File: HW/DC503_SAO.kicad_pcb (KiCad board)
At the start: 2 copper layers, 63.1 x 45.1 mm, 34 parts, among them J1 GS2, J2 GS2, U1 ATTINY85-20SU, X1 Badgelife_shitty_connector

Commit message: ROW3 and ROW_3 done.
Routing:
- net /ROW2: track 35.8 -> 90.4 mm, vias 0 -> 5
- net /ROW3: track 35.9 -> 85.7 mm
- net /ROW_2: track 73.2 -> 73.4 mm, vias 2 -> 4
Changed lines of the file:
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@@
   (general
     (links 38)
-    (no_connects 8)
+    (no_connects 4)
     (area 142.865544 64.023399 206.110001 109.234705)
     (thickness 1.6002)
     (drawings 335)
-    (tracks 141)
+    (tracks 170)
     (zones 0)
     (modules 34)
@@
     (37 F.SilkS user)
     (38 B.Mask user)
-    (39 F.Mask user)
+    (39 F.Mask user hide)
     (40 Dwgs.User user)
     (41 Cmts.User user)
@@
   (gr_line (start 205.4289 69.7478) (end 205.4621 69.7962) (layer Edge.Cuts) (width 0.1))
   (gr_line (start 204.5 75.5) (end 204.3829 75.8431) (layer Edge.Cuts) (width 0.1))
+  (segment (start 180 104.25) (end 176.25 104.25) (width 0.3048) (layer B.Cu) (net 1) (status 400000))
+  (via (at 156.6 100.2) (size 0.6858) (drill 0.3302) (layers F.Cu B.Cu) (net 1))
+  (segment (start 156.6 103.6) (end 156.6 100.2) (width 0.3048) (layer B.Cu) (net 1))
+  (segment (start 161.6 108.4) (end 156.6 103.6) (width 0.3048) (layer B.Cu) (net 1))
+  (segment (start 174.2 108.4) (end 161.6 108.4) (width 0.3048) (layer B.Cu) (net 1))
+  (via (at 174.2 108.4) (size 0.6858) (drill 0.3302) (layers F.Cu B.Cu) (net 1))
+  (segment (start 174.2 106.2) (end 174.2 108.4) (width 0.3048) (layer F.Cu) (net 1))
+  (segment (start 176.2 104.2) (end 174.2 106.2) (width 0.3048) (layer F.Cu) (net 1))
+  (via (at 176.2 104.2) (size 0.6858) (drill 0.3302) (layers F.Cu B.Cu) (net 1))
+  (segment (start 176.25 104.25) (end 176.2 104.2) (width 0.3048) (layer B.Cu) (net 1))
+  (segment (start 156.6 95.2) (end 156.6 100.2) (width 0.3048) (layer F.Cu) (net 1))
+  (segment (start 156.6 100.2) (end 156.6 97.8) (width 0.3048) (layer F.Cu) (net 1))
+  (via (at 156.6 95.2) (size 0.6858) (drill 0.3302) (layers F.Cu B.Cu) (net 1))
+  (segment (start 147.25 98.55) (end 147.25 93.25) (width 0.3048) (layer B.Cu) (net 1) (status 800000))
+  (segment (start 147.2 98.8) (end 147.25 98.55) (width 0.3048) (layer B.Cu) (net 1))
+  (via (at 147.2 98.8) (size 0.6858) (drill 0.3302) (layers F.Cu B.Cu) (net 1))
+  (segment (start 155.6 98.8) (end 147.2 98.8) (width 0.3048) (layer F.Cu) (net 1))
+  (segment (start 156.6 97.8) (end 155.6 98.8) (width 0.3048) (layer F.Cu) (net 1))
   (segment (start 150 70.5) (end 150 76.8) (width 0.3048) (layer B.Cu) (net 1))
-  (segment (start 147.25 79.55) (end 147.25 93.25) (width 0.3048) (layer B.Cu) (net 1))
   (segment (start 150 76.8) (end 147.25 79.55) (width 0.3048) (layer B.Cu) (net 1))
+  (segment (start 147.25 79.55) (end 147.25 93.25) (width 0.3048) (layer B.Cu) (net 1))
   (segment (start 159.25 88.2) (end 159.25 89.25) (width 0.3048) (layer B.Cu) (net 1))
   (segment (start 159.25 89.25) (end 159 89.5) (width 0.3048) (layer B.Cu) (net 1))
@@
   (segment (start 156.25 94.5) (end 156.6 95.2) (width 0.3048) (layer B.Cu) (net 1))
   (segment (start 156.6 95.2) (end 159.1 95.235) (width 0.3048) (layer B.Cu) (net 1))
-  (segment (start 163.5 75) (end 163.5 83.3) (width 0.3048) (layer B.Cu) (net 2))
+  (segment (start 192.5 81.75) (end 192.5 79.1) (width 0.3048) (layer B.Cu) (net 2) (status 400000))
+  (segment (start 191.2 77.8) (end 163.5 77.8) (width 0.3048) (layer B.Cu) (net 2))
+  (segment (start 192.5 79.1) (end 191.2 77.8) (width 0.3048) (layer B.Cu) (net 2))
+  (segment (start 148.75 81.75) (end 148.75 79.65) (width 0.3048) (layer B.Cu) (net 2) (status 400000))
+  (segment (start 150.6 77.8) (end 163.5 77.8) (width 0.3048) (layer B.Cu) (net 2))
+  (segment (start 148.75 79.65) (end 150.6 77.8) (width 0.3048) (layer B.Cu) (net 2))
+  (segment (start 163.5 75) (end 163.5 77.8) (width 0.3048) (layer B.Cu) (net 2))
+  (segment (start 163.5 77.8) (end 163.5 83.3) (width 0.3048) (layer B.Cu) (net 2))
   (segment (start 161.4 85.4) (end 161.4 91) (width 0.3048) (layer B.Cu) (net 2))
   (segment (start 163.5 83.3) (end 161.4 85.4) (width 0.3048) (layer B.Cu) (net 2))
@@
   (segment (start 153.25 99.35) (end 153.25 93.25) (width 0.3048) (layer B.Cu) (net 11))
   (segment (start 152.25 100.35) (end 153.25 99.35) (width 0.3048) (layer B.Cu) (net 11))
-  (segment (start 157.2 72.2) (end 157.2 80.8) (width 0.3048) (layer B.Cu) (net 12))
-  (via (at 157.2 80.8) (size 0.6858) (drill 0.3302) (layers F.Cu B.Cu) (net 12))
+  (segment (start 157.2 72.2) (end 157.2 76.4) (width 0.3048) (layer B.Cu) (net 12))
+  (via (at 157.2 76.4) (size 0.6858) (drill 0.3302) (layers F.Cu B.Cu) (net 12))
   (segment (start 156.3 86.3) (end 155.25 86.3) (width 0.3048) (layer B.Cu) (net 12))
   (via (at 157.2 85.6) (size 0.6858) (drill 0.3302) (layers F.Cu B.Cu) (net 12))
   (segment (start 156.3 86.3) (end 157.2 85.6) (width 0.3048) (layer B.Cu) (net 12))
-  (segment (start 157.2 80.8) (end 157.2 85.6) (width 0.3048) (layer F.Cu) (net 12))
+  (segment (start 157.2 76.4) (end 157.2 85.6) (width 0.3048) (layer F.Cu) (net 12))
   (segment (start 157.2 72.2) (end 157.2 72.3375) (width 0.3048) (layer B.Cu) (net 12))
   (segment (start 157.2 72.3375) (end 157.2 72.2) (width 0.3048) (layer B.Cu) (net 12))
@@
   (segment (start 168.3 72.7) (end 169.5 73.7) (width 0.3048) (layer B.Cu) (net 12))
   (segment (start 169.5 73.7) (end 169.5 75) (width 0.3048) (layer B.Cu) (net 12))
+  (segment (start 186.2 81) (end 186.8 80.2) (width 0.3048) (layer F.Cu) (net 13))
+  (via (at 186.2 81) (size 0.6858) (drill 0.3302) (layers F.Cu B.Cu) (net 13))
+  (segment (start 190.4 76) (end 190.25 76) (width 0.3048) (layer B.Cu) (net 13))
+  (via (at 190.4 76) (size 0.6858) (drill 0.3302) (layers F.Cu B.Cu) (net 13))
+  (segment (start 186.8 80.2) (end 190.4 76) (width 0.3048) (layer F.Cu) (net 13))
   (segment (start 161.75 81) (end 164.75 81) (width 0.3048) (layer F.Cu) (net 13))
   (via (at 161.75 81) (size 0.6858) (drill 0.3302) (layers F.Cu B.Cu) (net 13))
@@
   (segment (start 159.25 86.3) (end 159.25 83) (width 0.3048) (layer B.Cu) (net 13))
   (segment (start 190.25 76) (end 202.5 76) (width 0.3048) (layer B.Cu) (net 13))
-  (segment (start 186.2 81) (end 190.25 76) (width 0.3048) (layer B.Cu) (net 13))
   (segment (start 161.75 81) (end 161.75 81) (width 0.3048) (layer B.Cu) (net 13))
   (segment (start 164.75 81) (end 186.2 81) (width 0.3048) (layer B.Cu) (net 13))

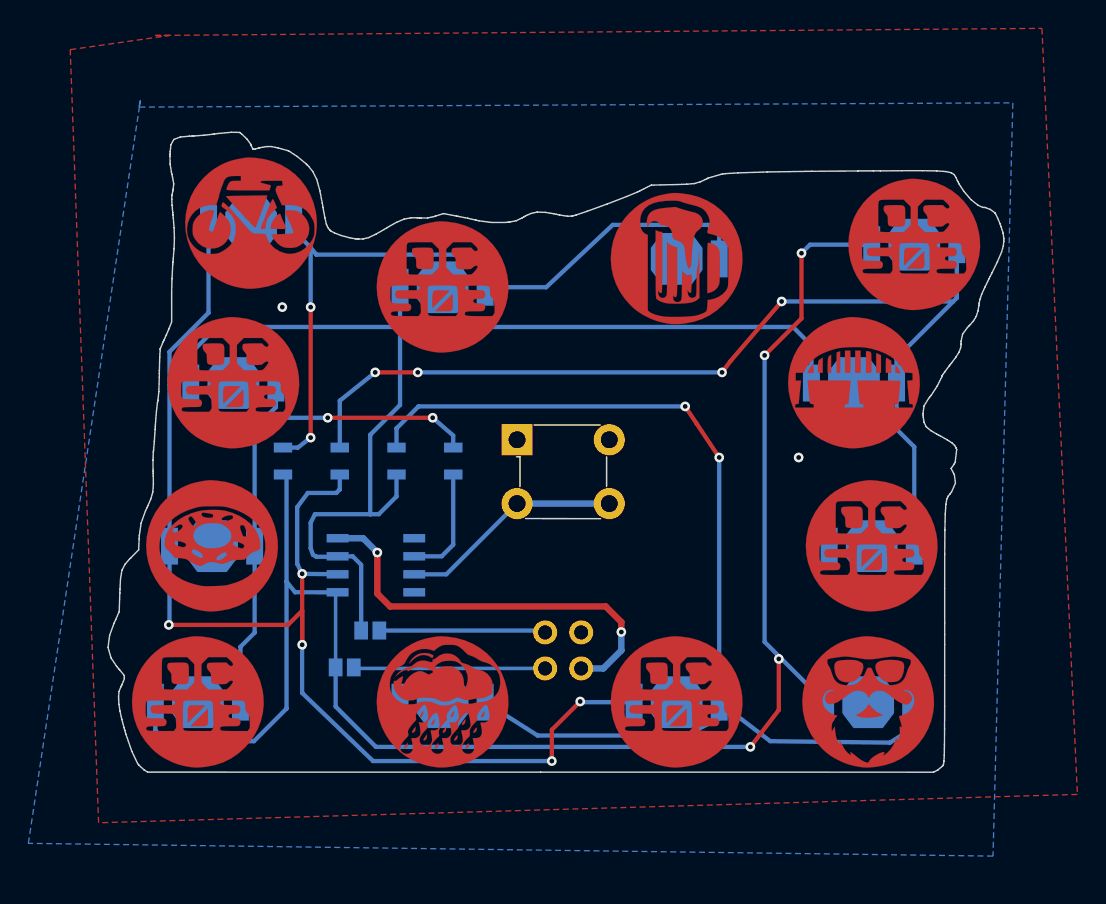
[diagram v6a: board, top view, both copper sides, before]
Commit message: ROW4 and ROW_4 done. touch up on other rows
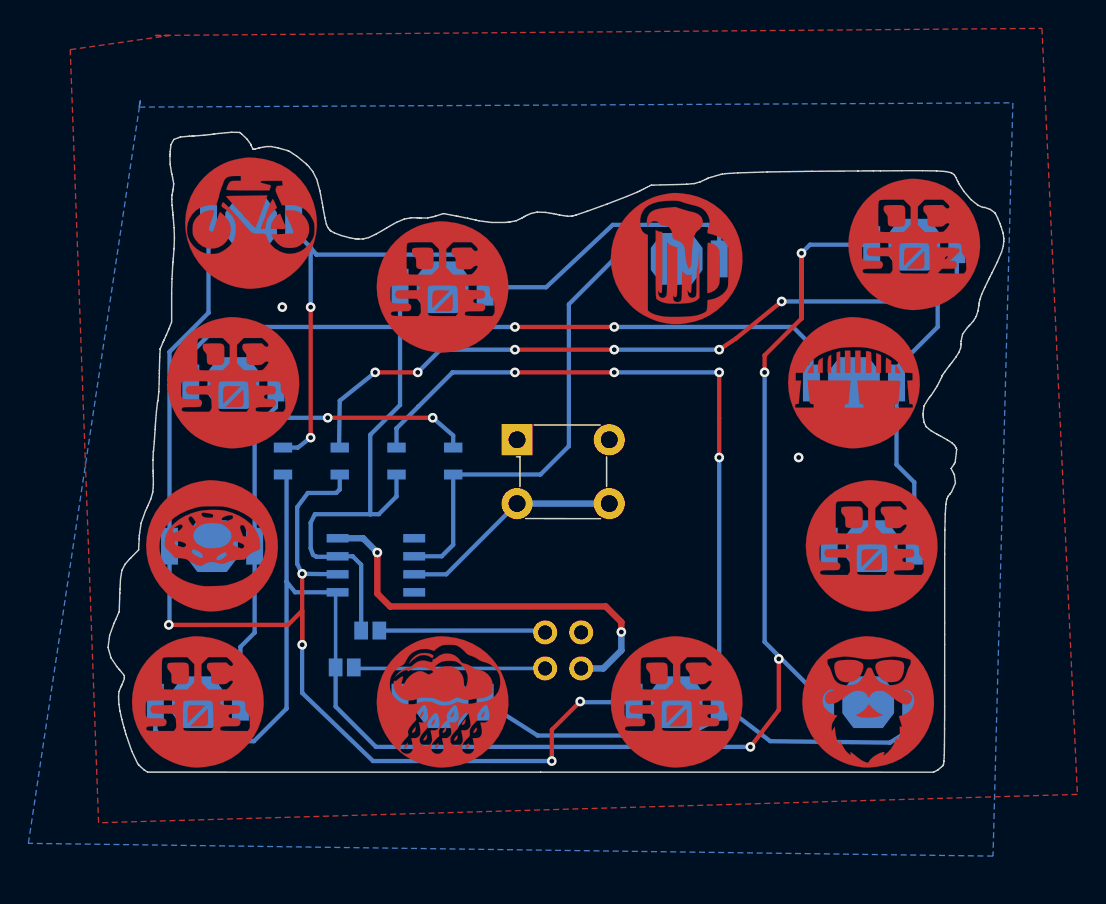
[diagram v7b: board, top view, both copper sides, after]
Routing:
- net /ROW4: track 8.04 -> 32.9 mm
- net (no net): track 0.00 -> 5.09 mm, vias 0 -> 2
- net /ROW_3: track 79.1 -> 84.2 mm, vias 2 -> 4
- net /ROW1: track 118.6 -> 123.2 mm
- net /ROW_2: track 73.4 -> 71.9 mm, vias 4 -> 6
- net /ROW3: vias 0 -> 2
- net GND: vias 2 -> 0

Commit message: finishing ground pours on back. KiCad keeps removing the vias from gnd connection
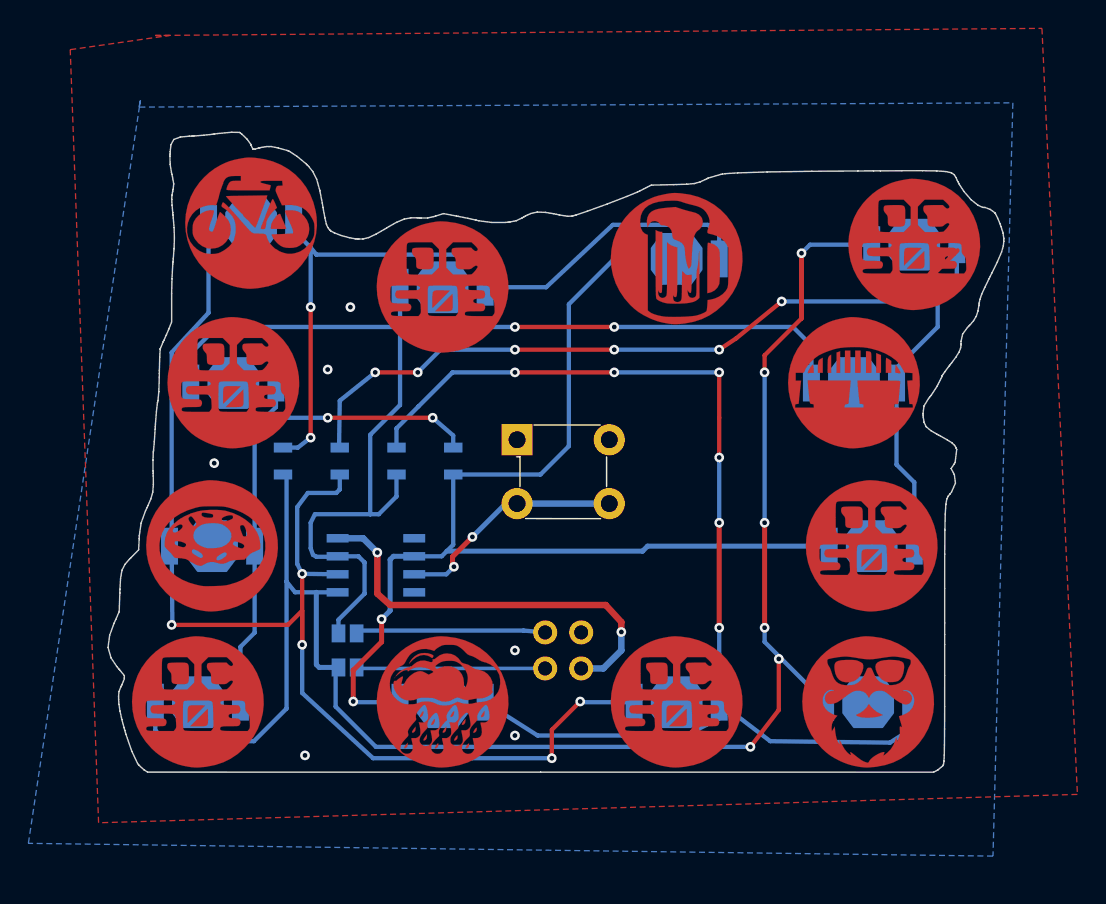
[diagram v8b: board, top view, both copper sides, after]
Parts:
- moved J1 1.61 mm to (159.8, 99.4)
- moved J2 0.20 mm to (159.8, 101.8)
- moved G*** 0.10 mm to (175.0, 89.4)
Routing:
- net /ROW4: track 32.9 -> 76.2 mm, vias 0 -> 2
- net /ROW1: track 123.2 -> 124.7 mm, vias 4 -> 6
- net Net-(J1-Pad2): track 11.7 -> 13.1 mm
- net /ROW3: track 85.7 -> 87.0 mm
- net /BUTTON: track 15.8 -> 16.6 mm, vias 0 -> 2
- net /ROW2: track 90.4 -> 89.7 mm
- net /ROW_3: vias 4 -> 6
- net GND: vias 0 -> 6
- net (no net): vias 2 -> 0
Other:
- board text added: "@Chris_Gammell"
- board text added: "@oshpark"
- board text added: "@securelyfitz"
- board text added: "By @office_deskjet https://git.io/fNaaO"
- board text added: "Thank you:"
